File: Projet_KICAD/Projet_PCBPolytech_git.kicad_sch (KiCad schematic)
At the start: 14 parts, among them J1 Conn_01x05_Socket, J2 USB_B_Micro, SW1 SW_Push, U1 STM32F446RETx, U2 USBLC6-2SC6

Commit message: Update Projet_PCBPolytech_git.kicad_sch
Mise à jour du schéma STM32F405 et alimentation
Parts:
- added C10, C11, C12, C9: 100n, Capacitor_SMD:C_0805_2012Metric, symbol Device:C
- added C13: 4.7u, Capacitor_SMD:C_0805_2012Metric, symbol Device:C
- added C4, C6: 100n, C_0805_2012Metric, symbol Device:C
- added C5: 1u, Capacitor_SMD:C_0805_2012Metric, symbol Device:C
- added C7, C8: 2.2u, Capacitor_SMD:C_0805_2012Metric, symbol Device:C
- added J3: Conn_01x14, symbol Connector_Generic:Conn_01x14
- added J4: Conn_01x04, symbol Connector_Generic:Conn_01x04
- U1: value STM32F446RETx -> STM32F405RGTx; symbol MCU_ST_STM32F4:STM32F446RETx -> MCU_ST_STM32F4:STM32F405RGTx; LCSC Part # (none) -> C15742
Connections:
- net +3V3: now also U1.1 (VBAT), U1.13 (VDDA), U1.19 (VDD), U1.32 (VDD), U1.48 (VDD), U1.64 (VDD), C10.1, C11.1, C12.1, C13.1, C4.1, C5.1, C6.1, C9.1
- net GND: now also C10.2, C11.2, C12.2, C13.2, C4.2, C5.2, C6.2, C7.1, C8.2, C9.2, J3.2 (Pin_2)
- net at U1.12 (VSSA): now also U1.18 (VSS), U1.63 (VSS)
- net at U1.31 (VCAP_1), U1.47 (VCAP_2): now also U1.3 (PC14), U1.4 (PC15), C7.2, C8.1; no longer U1.18 (VSS), U1.63 (VSS)
- net TFT_MISO: now reaches U1.21 (PA5)
- net TFT_MISO: now also U1.22 (PA6), U1.23 (PA7), J3.7 (Pin_7), J3.9 (Pin_9)
- net SD_CS: now reaches U1.29 (PB10)
- net SD_CS: now also U1.30 (PB11), U1.33 (PB12), U1.34 (PB13), U1.35 (PB14), U1.36 (PB15), U1.62 (PB9), J3.3 (Pin_3), J3.4 (Pin_4), J3.5 (Pin_5), J4.1 (Pin_1), J4.2 (Pin_2), J4.3 (Pin_3), J4.4 (Pin_4)
- new net LCD_VCC: J3.1 (Pin_1)
- new net TFT_LED: J3.8 (Pin_8)
- new net TFT_MOSI: J3.6 (Pin_6)
- new net TP_CLK: J3.10 (Pin_10)
- new net TP_CS: J3.11 (Pin_11)
- new net TP_DIN: J3.12 (Pin_12)
- new net TP_IRQ: J3.14 (Pin_14)
- new net TP_OUT: J3.13 (Pin_13)
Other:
- moved on the sheet: TP1

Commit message: Correction des condensateurs VCAP du STM32
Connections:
- new net: C7.2, U1.31 (VCAP_1)
- new net: C8.1, U1.47 (VCAP_2)
- now unconnected: U1.3 (PC14), U1.4 (PC15)
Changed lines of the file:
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@@
-	)
-	(junction
-		(at 115.57 153.67)
-		(diameter 0)
-		(color 0 0 0 0)
-	)
-	(junction
-		(at 93.98 153.67)
-		(diameter 0)
-		(color 0 0 0 0)
 	)
 	(junction
@@
 	)
 	(junction
-		(at 93.98 148.59)
-		(diameter 0)
-		(color 0 0 0 0)
-	)
-	(junction
 		(at 130.81 27.94)
 		(diameter 0)
@@
 	)
 	(junction
-		(at 115.57 156.21)
-		(diameter 0)
-		(color 0 0 0 0)
-	)
-	(junction
 		(at 130.81 46.99)
 		(diameter 0)
@@
 	)
 	(junction
-		(at 118.11 148.59)
-		(diameter 0)
-		(color 0 0 0 0)
-	)
-	(junction
 		(at 166.37 27.94)
 		(diameter 0)
@@
 	(wire
 		(pts
-			(xy 115.57 158.75) (xy 115.57 156.21)
-		)
-		(stroke
-			(width 0)
-			(type default)
-		)
-	)
-	(wire
-		(pts
 			(xy 34.29 104.14) (xy 34.29 106.68)
 		)
@@
 	(wire
 		(pts
-			(xy 118.11 146.05) (xy 118.11 148.59)
-		)
-		(stroke
-			(width 0)
-			(type default)
-		)
-	)
-	(wire
-		(pts
 			(xy 167.64 158.75) (xy 168.91 158.75)
 		)
@@
 	(wire
 		(pts
-			(xy 115.57 156.21) (xy 115.57 153.67)
-		)
-		(stroke
-			(width 0)
-			(type default)
-		)
-	)
-	(wire
-		(pts
 			(xy 215.9 151.13) (xy 223.52 151.13)
 		)
@@
 	(wire
 		(pts
-			(xy 93.98 148.59) (xy 118.11 148.59)
-		)
-		(stroke
-			(width 0)
-			(type default)
-		)
-	)
-	(wire
-		(pts
 			(xy 168.91 158.75) (xy 168.91 163.83)
 		)
@@
 	(wire
 		(pts
-			(xy 118.11 140.97) (xy 115.57 156.21)
-		)
-		(stroke
-			(width 0)
-			(type default)
-		)
-	)
-	(wire
-		(pts
-			(xy 118.11 148.59) (xy 118.11 158.75)
-		)
-		(stroke
-			(width 0)
-			(type default)
-		)
-	)
-	(wire
-		(pts
 			(xy 172.72 100.33) (xy 179.07 100.33)
 		)
@@
 	(wire
 		(pts
+			(xy 93.98 146.05) (xy 118.11 146.05)
+		)
+		(stroke
+			(width 0)
+			(type default)
+		)
+	)
+	(wire
+		(pts
+			(xy 115.57 153.67) (xy 115.57 148.59)
+		)
+		(stroke
+			(width 0)
+			(type default)
+		)
+	)
+	(wire
+		(pts
 			(xy 130.81 46.99) (xy 139.7 46.99)
 		)
@@
 	(wire
 		(pts
-			(xy 93.98 148.59) (xy 93.98 153.67)
-		)
-		(stroke
-			(width 0)
-			(type default)
-		)
-	)
-	(wire
-		(pts
 			(xy 162.56 148.59) (xy 163.83 148.59)
 		)
@@
 	(wire
 		(pts
-			(xy 93.98 146.05) (xy 93.98 148.59)
-		)
-		(stroke
-			(width 0)
-			(type default)
-		)
-	)
-	(wire
-		(pts
 			(xy 170.18 161.29) (xy 170.18 163.83)
 		)
@@
 	(wire
 		(pts
+			(xy 115.57 148.59) (xy 118.11 148.59)
+		)
+		(stroke
+			(width 0)
+			(type default)
+		)
+	)
+	(wire
+		(pts
 			(xy 170.18 27.94) (xy 170.18 60.96)
 		)
@@
 	(wire
 		(pts
-			(xy 118.11 138.43) (xy 115.57 153.67)
-		)
-		(stroke
-			(width 0)
-			(type default)
-		)
-	)
-	(wire
-		(pts
 			(xy 158.75 151.13) (xy 163.83 151.13)
 		)
@@
 		)
 		(stroke
-			(width 0)
-			(type default)
-		)
-	)
-	(wire
-		(pts
-			(xy 118.11 158.75) (xy 115.57 158.75)
-		)
-		(stroke

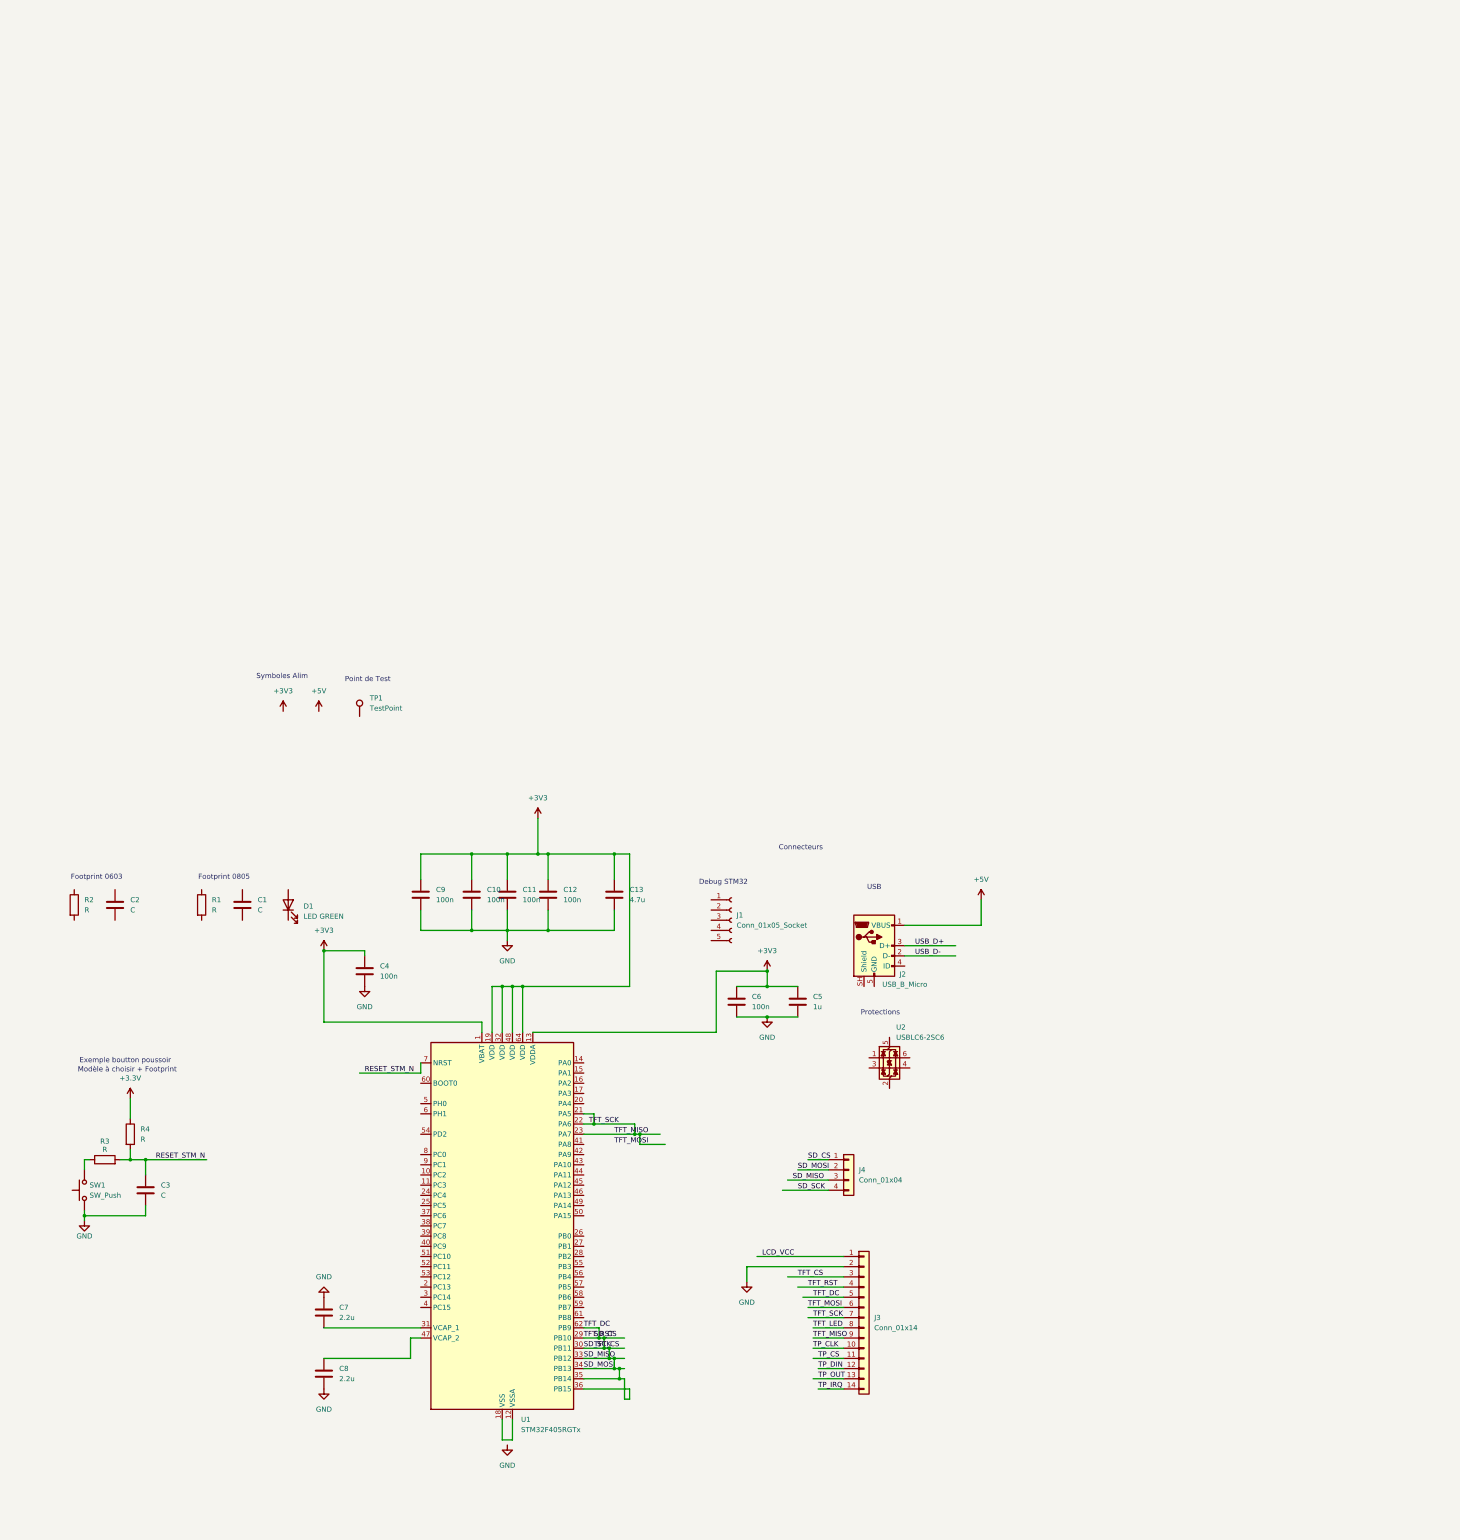
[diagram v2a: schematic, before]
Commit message: Update KiCad schematic and add STM32CubeMX configuration
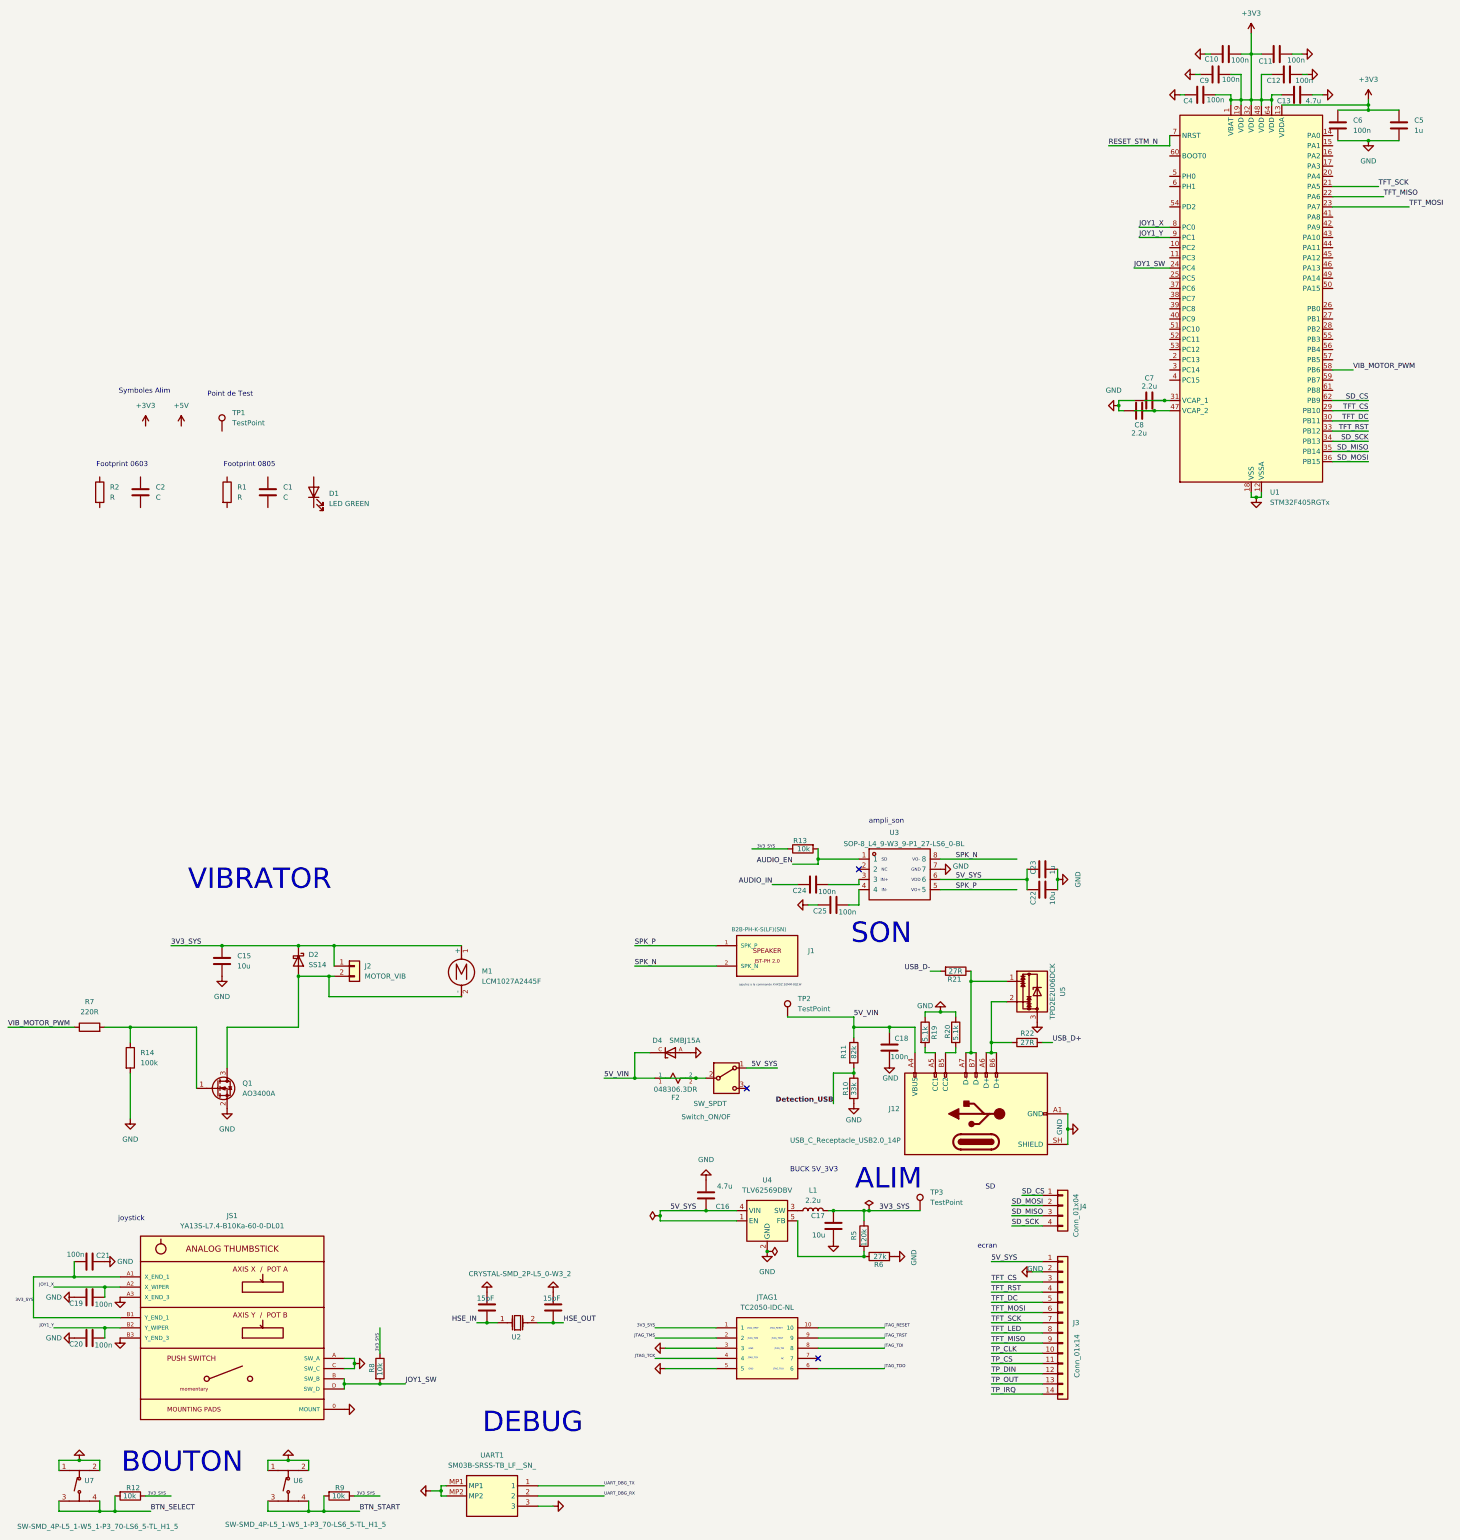
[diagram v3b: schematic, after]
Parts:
- removed C3: C, Capacitor_SMD:C_0805_2012Metric, symbol Device:C
- removed J1: Conn_01x05_Socket, Connector_PinHeader_2.54mm:PinHeader_1x05_P2.54mm_Vertical, symbol Connector:Conn_01x05_Socket
- removed J2: USB_B_Micro, Connector_USB:USB_Micro-AB_Molex_47590-0001, symbol Connector:USB_B_Micro
- removed R3, R4: R, Resistor_SMD:R_0805_2012Metric, symbol Device:R
- removed SW1: SW_Push, Button_Switch_SMD:SW_Push_1P1T_NO_CK_KSC6xxG, symbol Switch:SW_Push
- removed U2: USBLC6-2SC6, Package_TO_SOT_SMD:SOT-23-6_Handsoldering, symbol Power_Protection:USBLC6-2SC6
- added C14, C26: 15pF, Capacitor_SMD:C_0603_1608Metric, symbol Device:C
- added C15, C17, C22: 10u, Capacitor_SMD:C_0805_2012Metric, symbol Device:C
- added C16: 4.7u, Capacitor_SMD:C_0805_2012Metric, symbol Device:C
- added C18: 100n, Capacitor_SMD:C_0603_1608Metric, symbol Device:C
- added C19, C20, C21, C24, C25: 100n, Capacitor_SMD:C_0805_2012Metric, symbol Device:C
- added C23: 1u, Capacitor_SMD:C_0805_2012Metric, symbol Device:C
- added D2: SS14, Diode_SMD:D_SMA, symbol Diode:SS14
- added D4: SMBJ15A, diode_TVS:DIOM4336X265N, symbol diode_TVS:SMBJ15A
- added F2: 048306.3DR, fusible:Fuse_Littelfuse_483_1206, symbol fusible:048306.3DR
- added J1: B2B-PH-K-S(LF)(SN), Audio_GameBoy:JST_PH_B2B-PH-K_1x02_P2.00mm_Vertical, symbol Audio_GameBoy:JST_PH_2PIN_SPEAKER
- added J12: USB_C_Receptacle_USB2.0_14P, Capteurs_Parking:USB-C_perso, symbol Connector:USB_C_Receptacle_USB2.0_14P
- added J2: MOTOR_VIB, Connector_Wire:SolderWire-0.1sqmm_1x02_P3.6mm_D0.4mm_OD1mm_Relief, symbol Connector_Generic:Conn_01x02
- added JS1: YA13S-L7.4-B10Ka-60-0-DL01, Joystick_YTL:RES-ADJ-TH_YA13S-L7.4-B10KA-60-0-DL01, symbol Joystick_YTL_C37323748:YA13S-L7.4-B10Ka-60-0-DL01
- added JTAG1: TC2050-IDC-NL, jtag:TAG-CONNECT_TC2050-IDC-NL, symbol jtagfaceid:TC2050-IDC-NL
- added L1: 2.2u, Inductor_SMD:L_Bourns-SRN4018, symbol Device:L
- added M1: LCM1027A2445F, symbol Motor:Motor_DC
- added Q1: AO3400A, Package_TO_SOT_SMD:SOT-23, symbol Transistor_FET:AO3400A
- added R10: 33k, Resistor_SMD:R_0603_1608Metric, symbol Device:R
- added R11: 82k, Resistor_SMD:R_0603_1608Metric, symbol Device:R
- added R12, R13, R8, R9: 10k, Resistor_SMD:R_0805_2012Metric, symbol Device:R
- added R14: 100k, Resistor_SMD:R_0603_1608Metric, symbol Device:R
- added R19, R20: 5.1k, Resistor_SMD:R_0805_2012Metric, symbol Device:R
- added R21, R22: 27R, Resistor_SMD:R_0805_2012Metric, symbol Device:R
- added R5: 120k, Resistor_SMD:R_0805_2012Metric, symbol Device:R
- added R6: 27k, Resistor_SMD:R_0805_2012Metric, symbol Device:R
- added R7: 220R, Resistor_SMD:R_0603_1608Metric, symbol Device:R
- added Switch_ON/OF: SW_SPDT, Capteurs_Parking:Interrupteur_MT-0-102-A101-M200-RS, symbol Switch:SW_SPDT
- added TP2, TP3: TestPoint, TestPoint:TestPoint_Pad_D2.0mm, symbol Connector:TestPoint
- added U2: CRYSTAL-SMD_2P-L5_0-W3_2, symbol CRYSTAL-SMD_2P-L5_0-W3_2_TX50328M2FDCE1T_C5182763:CRYSTAL-SMD_2P-L5_0-W3_2
- added U3: SOP-8_L4_9-W3_9-P1_27-LS6_0-BL, symbol ampli_son:SOP-8_L4_9-W3_9-P1_27-LS6_0-BL
- added U4: TLV62569DBV, Package_TO_SOT_SMD:SOT-23-5, symbol Regulator_Switching:TLV62569DBV
- added U5: TPD2E2U06DCK, Package_TO_SOT_SMD:SOT-323_SC-70, symbol Power_Protection:TPD2E2U06DCK
- added U6, U7: SW-SMD_4P-L5_1-W5_1-P3_70-LS6_5-TL_H1_5, symbol bouton:SW-SMD_4P-L5_1-W5_1-P3_70-LS6_5-TL_H1_5
- added UART1: SM03B-SRSS-TB_LF__SN_, uart:SM03BSRSSTBLFSN, symbol uartfaceid:SM03B-SRSS-TB_LF__SN_
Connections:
- net +3V3: now also C10.2, C11.2, C4.2; no longer C10.1, C11.1, C4.1
- net GND: now also C10.1, C11.1, C4.1, C8.1, U1.12 (VSSA), U1.18 (VSS), U1.63 (VSS), C14.1, C15.2, C16.2, C17.2, C18.2, C19.2, C20.2, C21.2, C22.2, C23.2, C25.2, C26.1, D4.A, J12.A1 (GND), J12.A12 (GND), J12.B1 (GND), J12.B12 (GND), J12.SH (SHIELD), JS1.0 (MOUNT), JS1.A (SW_A), JS1.A3 (X_END_3), JS1.B3 (Y_END_3), JS1.C (SW_C), JTAG1.3, JTAG1.5, Q1.2 (S), R10.2, R14.2, R19.1, R20.1, R6.2, U3.7, U4.2 (GND), U5.3, U6.1, U6.2, U7.1, U7.2, UART1.3, UART1.MP1, UART1.MP2; no longer C10.2, C11.2, C4.2, C8.2
- net SD_CS: no longer J3.3 (Pin_3), J3.4 (Pin_4), J3.5 (Pin_5), J4.2 (Pin_2), J4.3 (Pin_3), J4.4 (Pin_4), U1.29 (PB10), U1.30 (PB11), U1.33 (PB12), U1.34 (PB13), U1.35 (PB14), U1.36 (PB15)
- net TFT_MISO: no longer J3.7 (Pin_7), U1.21 (PA5), U1.23 (PA7)
- net TFT_MOSI: now also U1.23 (PA7)
- net USB_D+: now also R22.2
- net USB_D-: now also R21.2
- net at U1.47 (VCAP_2): now also C8.2; no longer C8.1
- net JOY1_SW: now reaches U1.24 (PC4)
- net JOY1_SW: now also JS1.B (SW_B), JS1.D (SW_D), R8.2
- net VIB_MOTOR_PWM: now reaches U1.58 (PB6)
- net VIB_MOTOR_PWM: now also R7.1
- net JOY1_X: now reaches U1.8 (PC0)
- net JOY1_X: now also C19.1, JS1.A2 (X_WIPER)
- net JOY1_Y: now reaches U1.9 (PC1)
- net JOY1_Y: now also C20.1, JS1.B2 (Y_WIPER)
- net LCD_VCC renamed 5V_SYS
- net 5V_SYS: now also C16.1, C22.1, C23.1, Switch_ON/OF.1 (A), U3.6, U4.1 (EN), U4.4 (VIN)
- new net: F2.2, Switch_ON/OF.2 (B)
- new net: Q1.1 (G), R14.1, R7.2
- new net: C24.1, U3.3
- new net: C25.1, U3.4
- new net: J12.A6 (D+), J12.B6 (D+), R22.1, U5.2
- new net: D2.2 (A), J2.2 (Pin_2), M1.2 (-), Q1.3 (D)
- new net: L1.1, U4.3 (SW)
- new net: J12.B5 (CC2), R20.2
- new net: R5.2, R6.1, U4.5 (FB)
- new net: J12.A7 (D-), J12.B7 (D-), R21.1, U5.1
- new net: J12.A5 (CC1), R19.2
- new net 3V3_SYS: C15.1, C17.1, C21.1, D2.1 (K), J2.1 (Pin_1), JS1.A1 (X_END_1), JS1.B1 (Y_END_1), JTAG1.1, L1.2, M1.1 (+), R12.1, R13.1, R5.1, R8.1, R9.1, TP3.1
- new net 5V_VIN: C18.1, D4.C, F2.1, J12.A4 (VBUS), J12.A9 (VBUS), J12.B4 (VBUS), J12.B9 (VBUS), R11.1, TP2.1
- new net AUDIO_EN: R13.2, U3.1
- new net AUDIO_IN: C24.2
- new net BTN_SELECT: R12.2, U7.3, U7.4
- new net BTN_START: R9.2, U6.3, U6.4
- new net Detection_USB: R10.1, R11.2
- new net HSE_IN: C14.2, U2.1
- new net HSE_OUT: C26.2, U2.2
- new net JTAG_RESET: JTAG1.10
- new net JTAG_TCK: JTAG1.4
- new net JTAG_TDI: JTAG1.8
- new net JTAG_TDO: JTAG1.6
- new net JTAG_TMS: JTAG1.2
- new net JTAG_TRST: JTAG1.9
- new net SD_MISO: J4.3 (Pin_3), U1.35 (PB14)
- new net SD_MOSI: J4.2 (Pin_2), U1.36 (PB15)
- new net SD_SCK: J4.4 (Pin_4), U1.34 (PB13)
- new net SPK_N: J1.2 (SPK_N), U3.8
- new net SPK_P: J1.1 (SPK_P), U3.5
- new net TFT_CS: J3.3 (Pin_3), U1.29 (PB10)
- new net TFT_DC: J3.5 (Pin_5), U1.30 (PB11)
- new net TFT_RST: J3.4 (Pin_4), U1.33 (PB12)
- new net TFT_SCK: J3.7 (Pin_7), U1.21 (PA5)
- new net UART_DBG_RX: UART1.2
- new net UART_DBG_TX: UART1.1
- no-connect marks 0 -> 3
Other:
- note added: "ALIM"
- note added: "BOUTON"
- note added: "BUCK 5V_3V3"
- note added: "DEBUG"
- note added: "GND"
- note added: "IN+"
- note added: "IN-"
- note added: "JTAG_RESET"
- note added: "JTAG_TCK"
- note added: "JTAG_TDI"
- note added: "JTAG_TDO"
- note added: "JTAG_TMS"
- note added: "JTAG_TRST"
- note added: "JTAG_VREF"
- note added: "NC"
- note added: "SD"
- note added: "SON"
- note added: "VDD"
- note added: "VIBRATOR"
- note added: "VO+"
- note added: "VO-"
- note added: "ajoutez a la commande XHXDZ 20MM-8Ω1W"
- note added: "ampli_son"
- note added: "ecran"
- note added: "joystick"
- note removed: "Connecteurs"
- note removed: "Debug STM32"
- note removed: "Exemple boutton poussoir"
- note removed: "Modèle à choisir + Footprint"
- note removed: "Protections"
- note removed: "USB"
- moved on the sheet: C1, C10, C11, C12, C13, C2, C4, C5, C6, C7, C8, C9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

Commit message: Mise à jour schéma PCB et connexions STM32
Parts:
- removed C1: C, Capacitor_SMD:C_0805_2012Metric, symbol Device:C
- removed C2: C, Capacitor_SMD:C_0603_1608Metric, symbol Device:C
- removed D1: LED GREEN, LED_SMD:LED_0805_2012Metric, symbol Device:LED
- removed R2: R, Resistor_SMD:R_0603_1608Metric, symbol Device:R
- removed TP1: TestPoint, TestPoint:TestPoint_Pad_D2.0mm, symbol Connector:TestPoint
- added R_SD1: 10k, Resistor_SMD:R_0603_1608Metric, symbol Device:R
- R1: value R -> 10k; footprint Resistor_SMD:R_0805_2012Metric -> Resistor_SMD:R_0603_1608Metric
- renumbered Switch_ON/OF to Switch_ON/OF1
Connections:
- net 3V3_SYS is gone; now on net +3V3: C15.1, C17.1, C21.1, D2.1 (K), J2.1 (Pin_1), JS1.A1 (X_END_1), JS1.B1 (Y_END_1), JTAG1.1, L1.2, M1.1 (+), R12.1, R13.1, R5.1, R8.1, R9.1, TP3.1
- net JTAG_RESET is gone; now on net RESET_STM_N: JTAG1.10
- net TFT_LED is gone; now on net +3V3: J3.8 (Pin_8)
- net +3V3: now also R_SD1.1
- net BTN_SELECT: now also U1.37 (PC6)
- net BTN_START: now also U1.25 (PC5)
- net GND: now also R1.2
- net HSE_IN: now also U1.5 (PH0)
- net HSE_OUT: now also U1.6 (PH1)
- net JTAG_TCK: now also U1.49 (PA14)
- net JTAG_TMS: now also U1.46 (PA13)
- net SD_CS: now also R_SD1.2
- net TFT_MISO: no longer U1.22 (PA6)
- net TFT_MOSI: no longer U1.23 (PA7)
- net TFT_SCK: no longer U1.21 (PA5)
- net TP_CLK: now also U1.21 (PA5)
- net TP_CS: now also U1.38 (PC7)
- net TP_DIN: now also U1.23 (PA7)
- net TP_IRQ: now also U1.59 (PB7)
- net TP_OUT: now also U1.22 (PA6)
- net UART_DBG_RX: now also U1.17 (PA3)
- net UART_DBG_TX: now also U1.16 (PA2)
- net at U1.60 (BOOT0): now also R1.1
- no-connect marks 3 -> 30
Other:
- note removed: "Footprint 0603"
- note removed: "Footprint 0805"
- note removed: "Point de Test"
- note removed: "Symboles Alim"
- moved on the sheet: C10, C11, C12, C13, C4, C5, C6, C7, C8, C9, U1
